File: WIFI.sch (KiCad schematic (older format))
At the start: 67 parts, among them P701 WL_DBG, P702 WL_RS232, P703 BT_DBG, U701 U.FL, U702 U.FL, U703 WL1807MOD, U901 ESP-12E, Y701 ANT1/BT, Y702 ANT2/WL

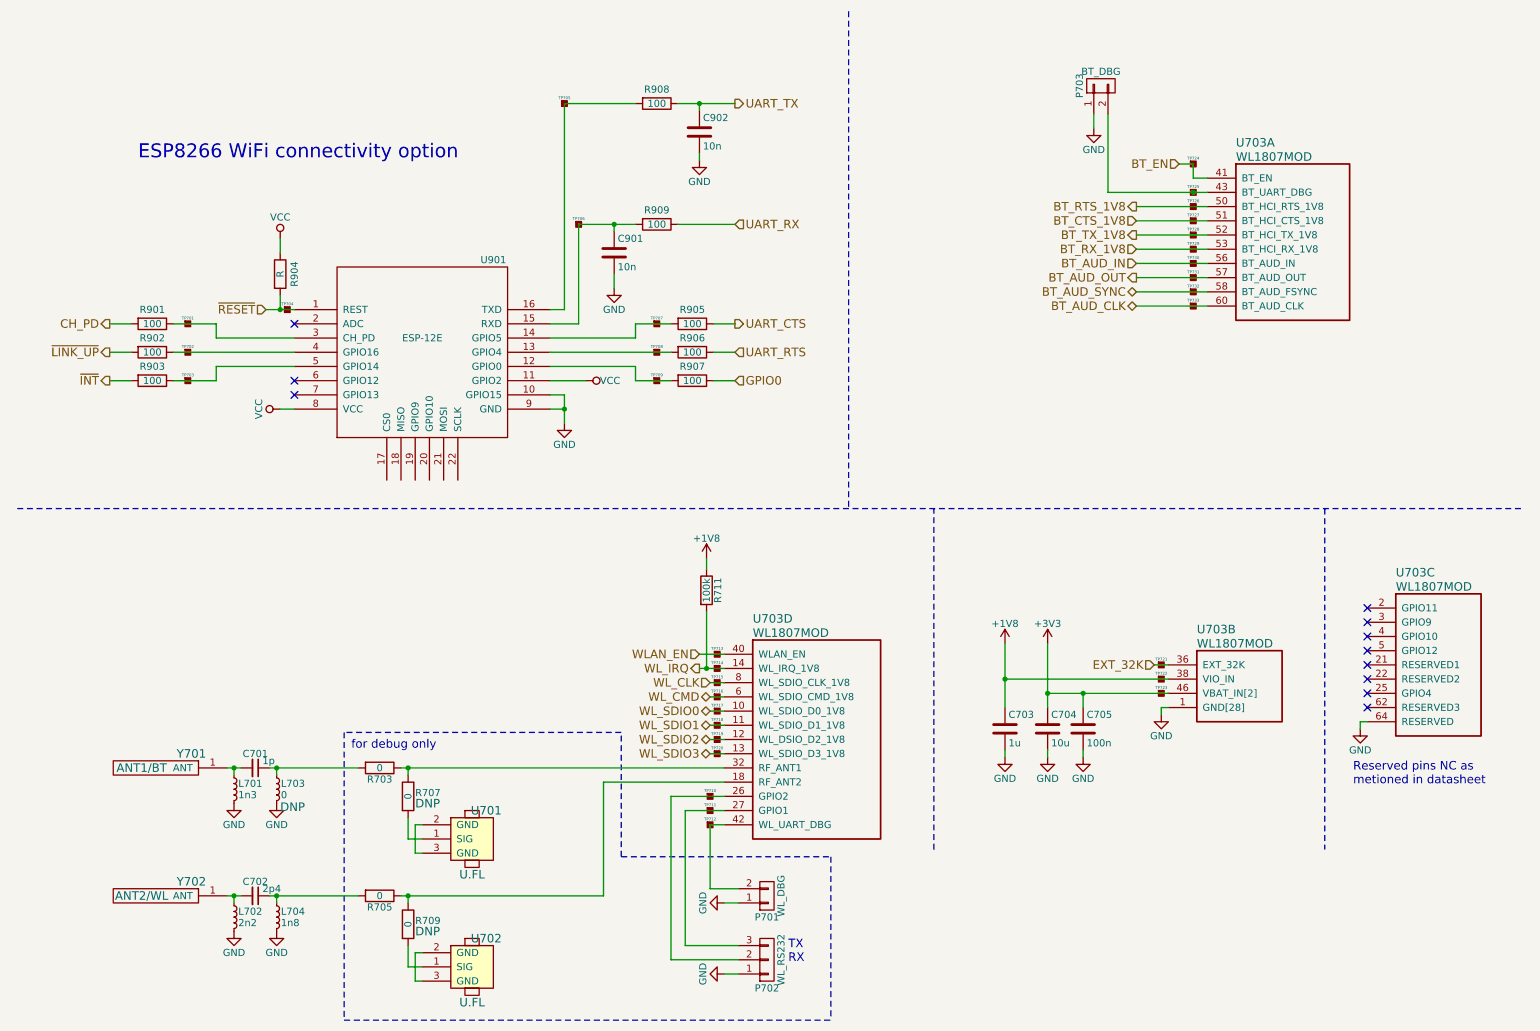
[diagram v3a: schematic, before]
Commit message: moved to some Bus routing for serveral communication signals on the top sheet. This reduces lines on the top sheet.
Changed 4V boost converter circuit toi use TPS61046 for size reasons
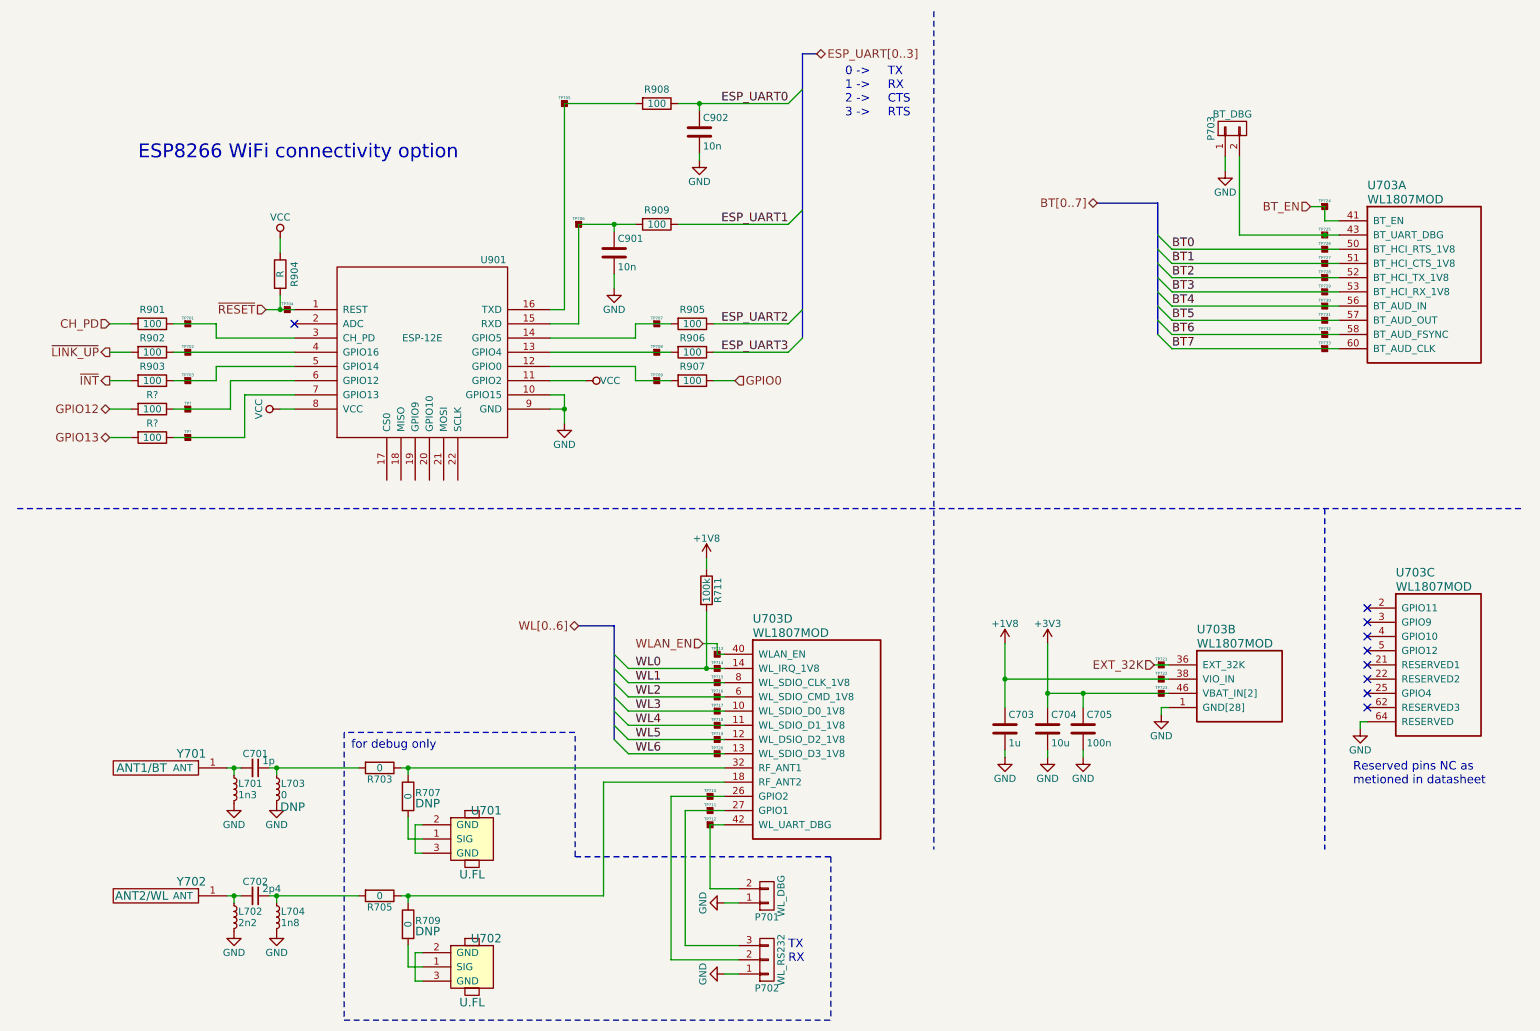
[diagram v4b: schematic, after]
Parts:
- added R? (x2): 100, symbol R
- added TP? (x2): TP, symbol TP
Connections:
- net WLAN_EN: now also TP713.1
- net at U901.6 (GPIO12): now also R?.1
- net at U901.7 (GPIO13): now also R?.1
- net BT_AUD_CLK renamed BT7
- net BT_AUD_IN renamed BT4
- net BT_AUD_OUT renamed BT5
- net BT_AUD_SYNC renamed BT6
- net BT_CTS_1V8 renamed BT1
- net BT_RTS_1V8 renamed BT0
- net BT_RX_1V8 renamed BT3
- net BT_TX_1V8 renamed BT2
- net UART_CTS renamed ESP_UART2
- net UART_RTS renamed ESP_UART3
- net UART_RX renamed ESP_UART1
- net UART_TX renamed ESP_UART0
- net WL_CLK renamed WL1
- net WL_CMD renamed WL2
- net WL_IRQ renamed WL0
- net WL_SDIO0 renamed WL3
- net WL_SDIO1 renamed WL4
- net WL_SDIO2 renamed WL5
- net WL_SDIO3 renamed WL6
- new net GPIO12: R?.2
- new net GPIO13: R?.2
- no-connect marks 11 -> 9
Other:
- note added: "0 ->\n1 ->\n2 ->\n3 ->\n"
- note added: "TX\nRX\nCTS\nRTS"
- moved on the sheet: P703, TP724, TP725, TP726, TP727, TP728, TP729, TP730, TP731, TP732, TP733, U703A

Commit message: aktuelle Version
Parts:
- C701, C702, C703, C704, C705, C901, C902: footprint (none) -> Capacitors_SMD:C_0603
- L701, L702, L703, L704, R711, R901, R902, R903, R904, R905, R906, R907, R908, R909: footprint (none) -> Resistors_SMD:R_0603
- P701, P703: footprint (none) -> Pin_Headers:Pin_Header_Straight_1x02
- P702: footprint (none) -> Pin_Headers:Pin_Header_Straight_1x03
- R601, R602: renamed from R?; footprint (none) -> Resistors_SMD:R_0603
- R703, R705, R707, R709: footprint Resistors_SMD:R_0402 -> Resistors_SMD:R_0603
- TP601, TP602: renamed from TP?; footprint (none) -> buttons:TP
- TP701, TP702, TP703, TP704, TP705, TP706, TP707, TP708, TP709, TP710, TP711, TP712, TP713, TP714, TP715, TP716, TP717, TP718, TP719, TP720, TP721, TP722, TP723, TP724, TP725, TP726, TP727, TP728, TP729, TP730, TP731, TP732, TP733: footprint (none) -> buttons:TP
- U701, U702: footprint (none) -> buttons:Foil_Button
